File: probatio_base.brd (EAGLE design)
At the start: 50 x 50 mm, 13 parts

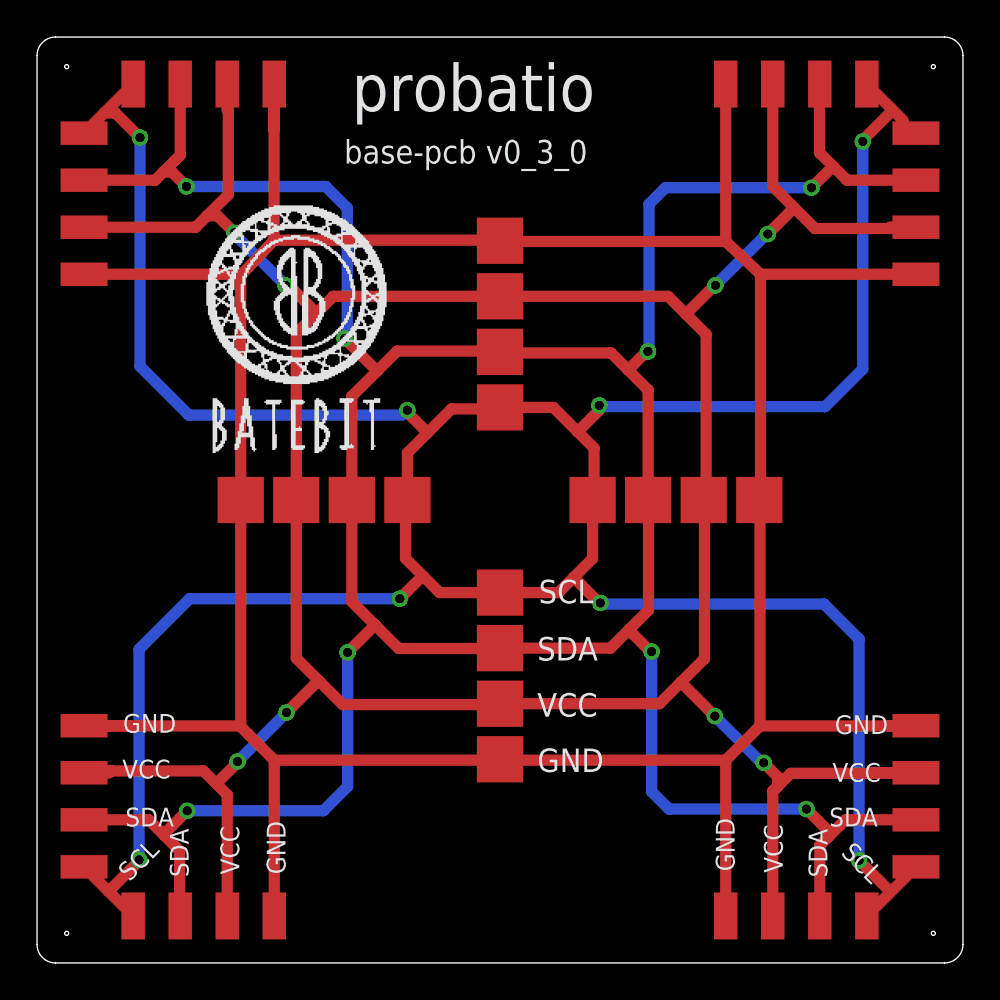
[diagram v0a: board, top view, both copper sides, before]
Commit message: Bug fix: changing layers of pads
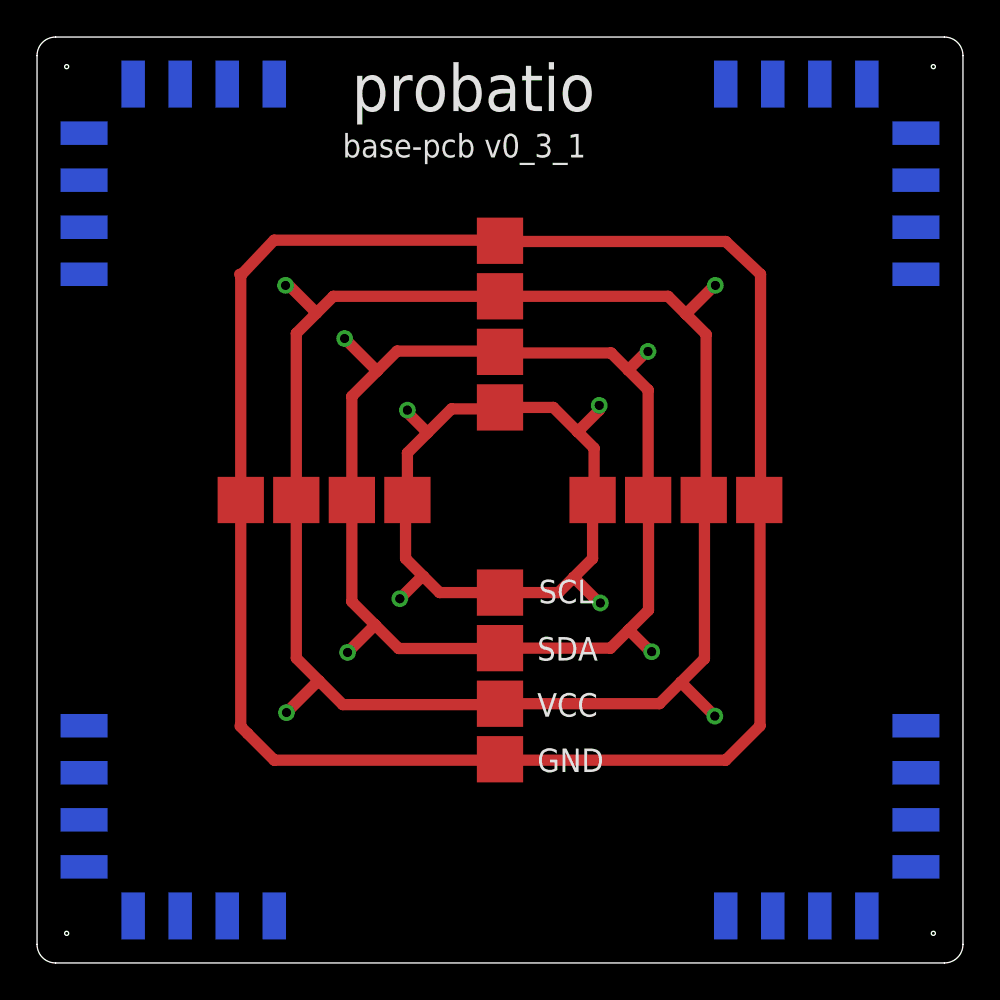
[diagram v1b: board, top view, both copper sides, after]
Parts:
- moved U$13 13.9 mm to (25.0, 26.6), flipped to the bottom
- flipped U$10 to the bottom, turned to 270 degrees
- flipped U$11 to the bottom, turned to 90 degrees
- flipped U$12 to the bottom
- flipped U$5 to the bottom, turned to 270 degrees
- flipped U$6 to the bottom, turned to 90 degrees
- flipped U$7 to the bottom
- flipped U$8 to the bottom
- flipped U$9 to the bottom
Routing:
- net SCL: track 176.2 -> 42.7 mm, vias 8 -> 4
- net SDA: track 178.3 -> 67.0 mm, vias 8 -> 4
- net VCC: track 180.5 -> 92.5 mm, vias 8 -> 4
- net GND: track 183.5 -> 109.8 mm
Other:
- board text added: "base-pcb v0_3_1"
- board text removed: "base-pcb v0_3_0"

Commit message: Update probatio_base.brd
Last adjustments for 0.3.1
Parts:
- turned U$10 to 90 degrees
- turned U$11 to 270 degrees
- turned U$12 to 0 degrees
- turned U$5 to 90 degrees
- turned U$6 to 270 degrees
- turned U$7 to 180 degrees
- turned U$8 to 180 degrees
- turned U$9 to 0 degrees
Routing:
- net SCL: track 42.7 -> 204.6 mm
- net SDA: track 67.0 -> 202.4 mm
- net VCC: track 92.5 -> 198.7 mm
- net GND: track 109.8 -> 169.0 mm, vias 0 -> 4
